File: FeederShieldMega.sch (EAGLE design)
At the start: 29 parts, among them J1 Digital_0_7, J10 Power, J11 M02X5-SHROUDED, J12 M02X5-SHROUDED, J13 M02X5-SHROUDED, J14 M02X5-SHROUDED, J15 M02X5-SHROUDED, J16 M02X5-SHROUDED, J2 Analog, J3 Digital_8_13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

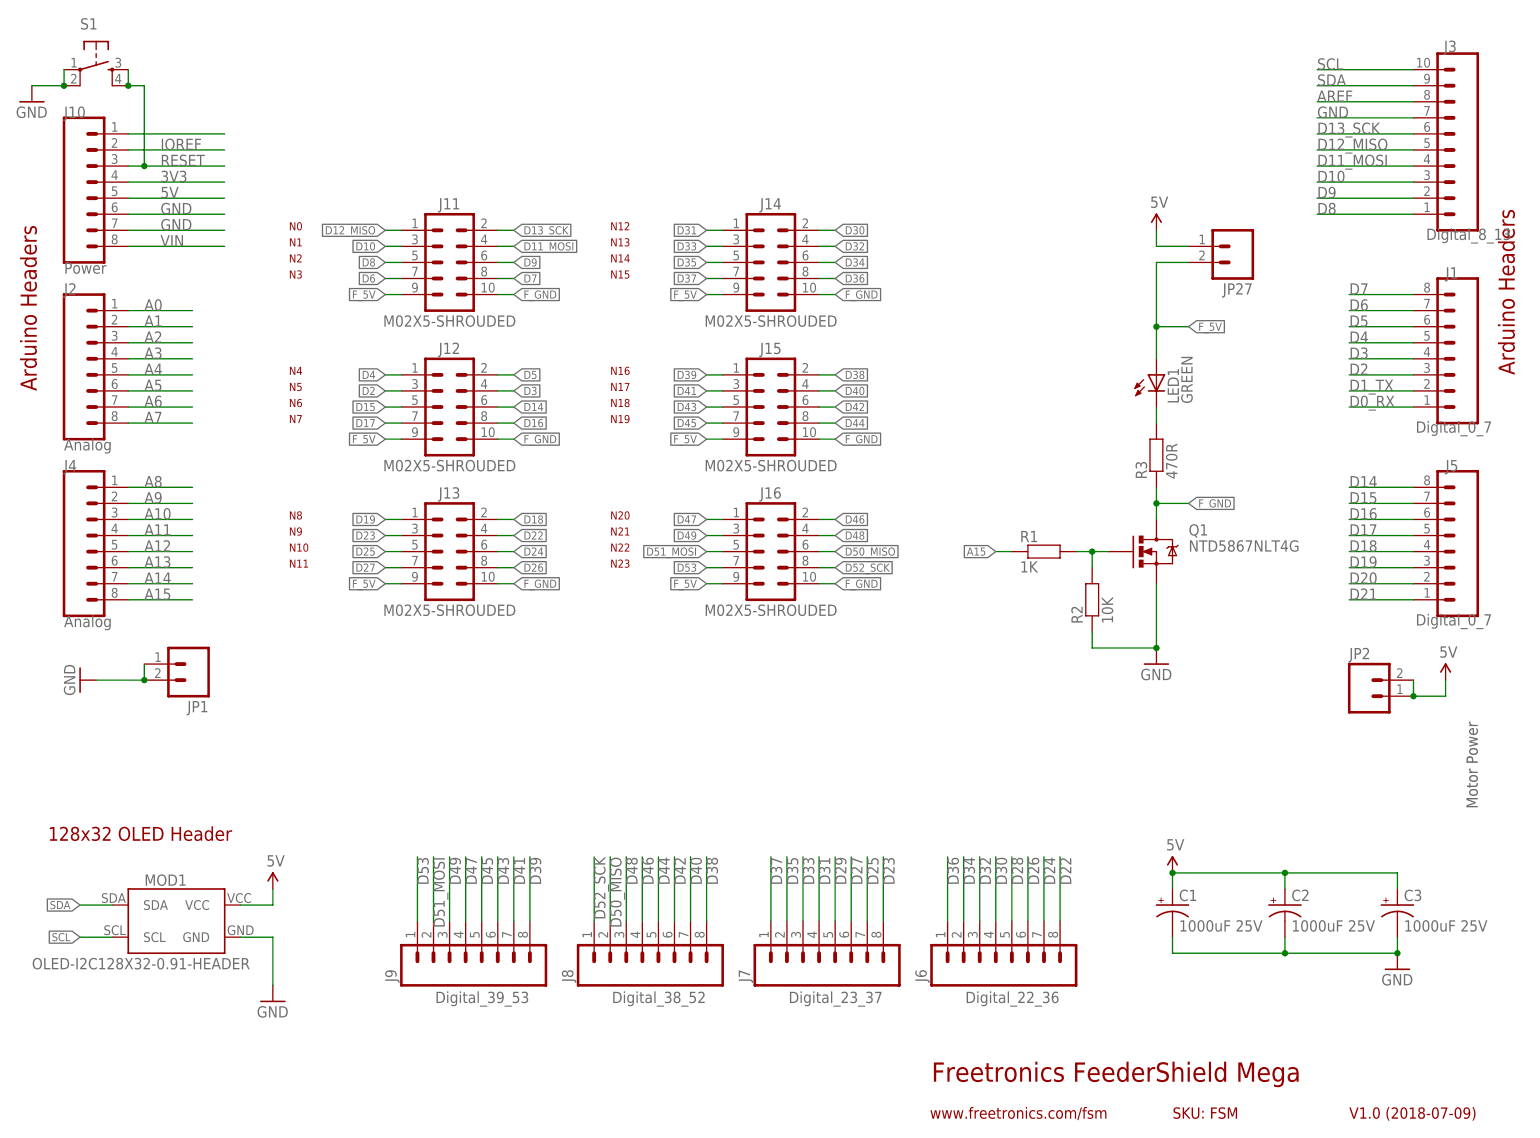
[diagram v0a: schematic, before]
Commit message: Added 5V 3A voltage regulator and removed 2 bulk decoupling caps for v3.0 release
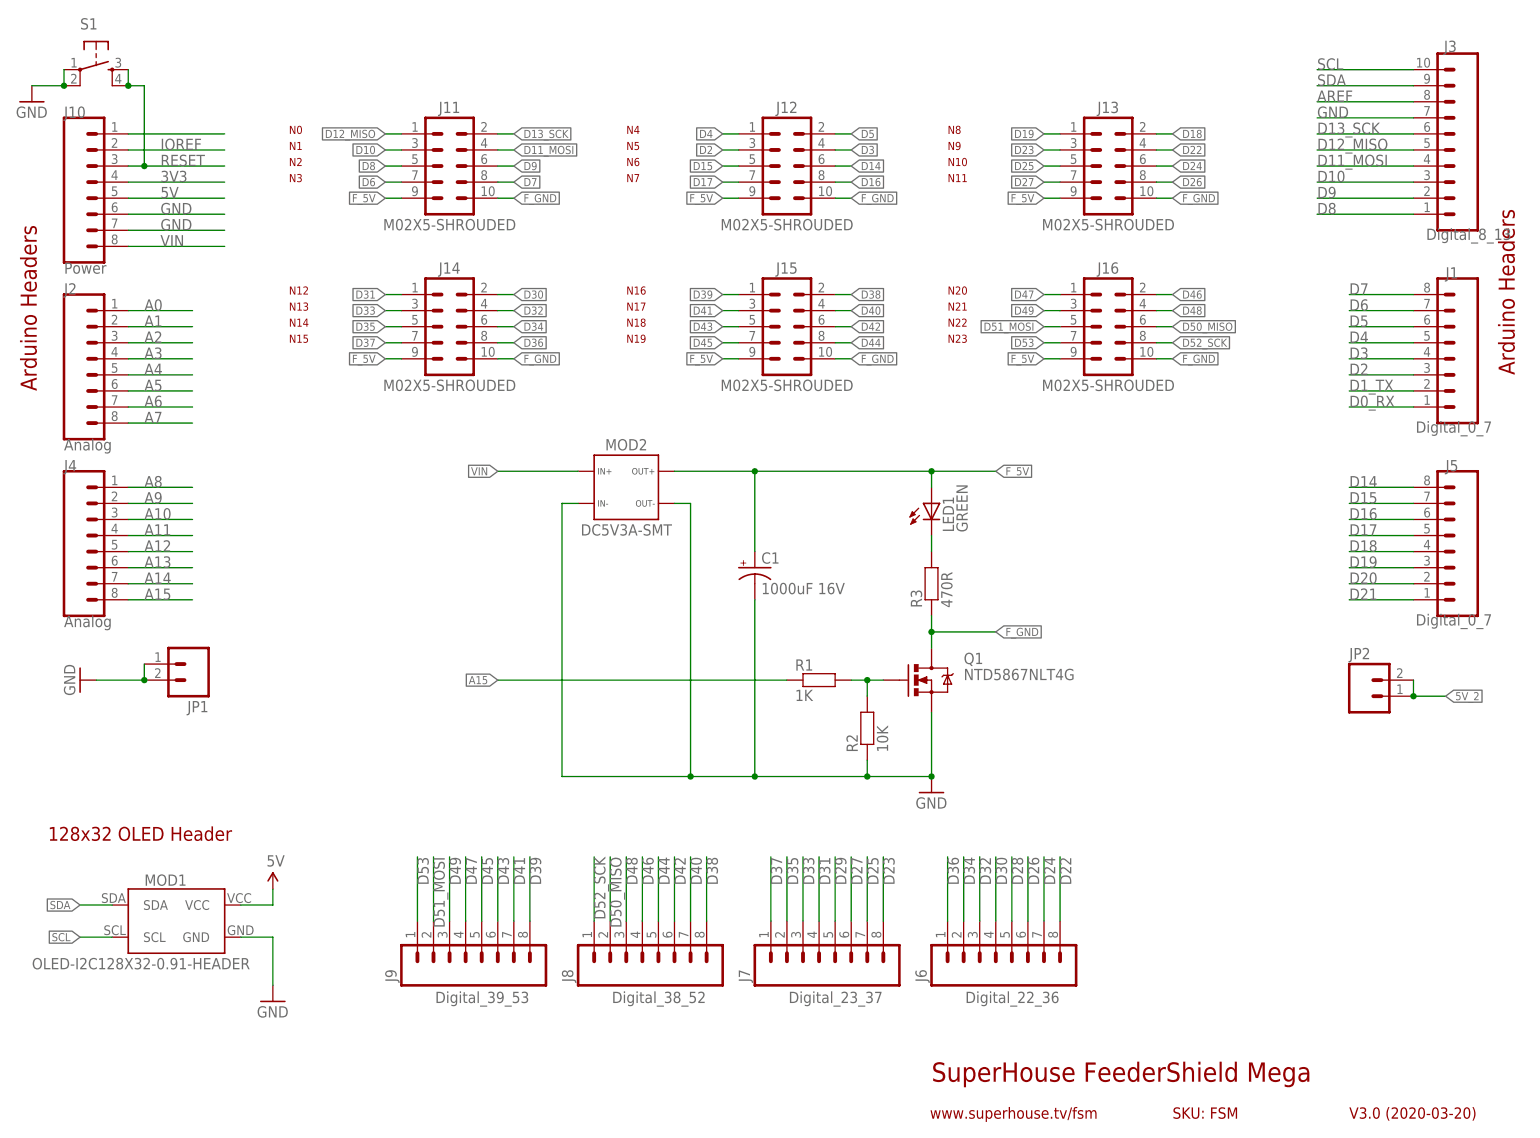
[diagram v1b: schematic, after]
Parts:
- removed C2, C3: 1000uF 25V, SuperHouse-DiscreteSemi:CAP_POL-5.08-10X18-FLAT
- removed JP27: (no value), SuperHouse-Connectors:M02-PIN
- added MOD2: DC5V3A-SMT, SuperHouse-Regulators:DC5V3A-SMT
- C1: value 1000uF 25V -> 1000uF 16V
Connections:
- new net 5V_2: JP2.1, JP2.2
- net 5V: no longer C1.+, C2.+, C3.+, JP2.1, JP2.2, JP27.1
- net F_5V: now also C1.+, MOD2.3; no longer JP27.2
- net GND: now also MOD2.1, MOD2.4; no longer C2.-, C3.-
- net VIN: now also MOD2.2
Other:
- note added: "SuperHouse FeederShield Mega"
- note added: "V3.0 (2020-03-20)"
- note added: "www.superhouse.tv/fsm"
- note removed: "Freetronics FeederShield Mega"
- note removed: "Motor Power"
- note removed: "V1.0 (2018-07-09)"
- note removed: "www.freetronics.com/fsm"
- moved on the sheet: C1, J11, J12, J13, J14, J15, J16, LED1, Q1, R1, R2, R3
